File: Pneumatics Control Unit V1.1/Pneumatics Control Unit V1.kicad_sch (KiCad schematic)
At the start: 52 parts

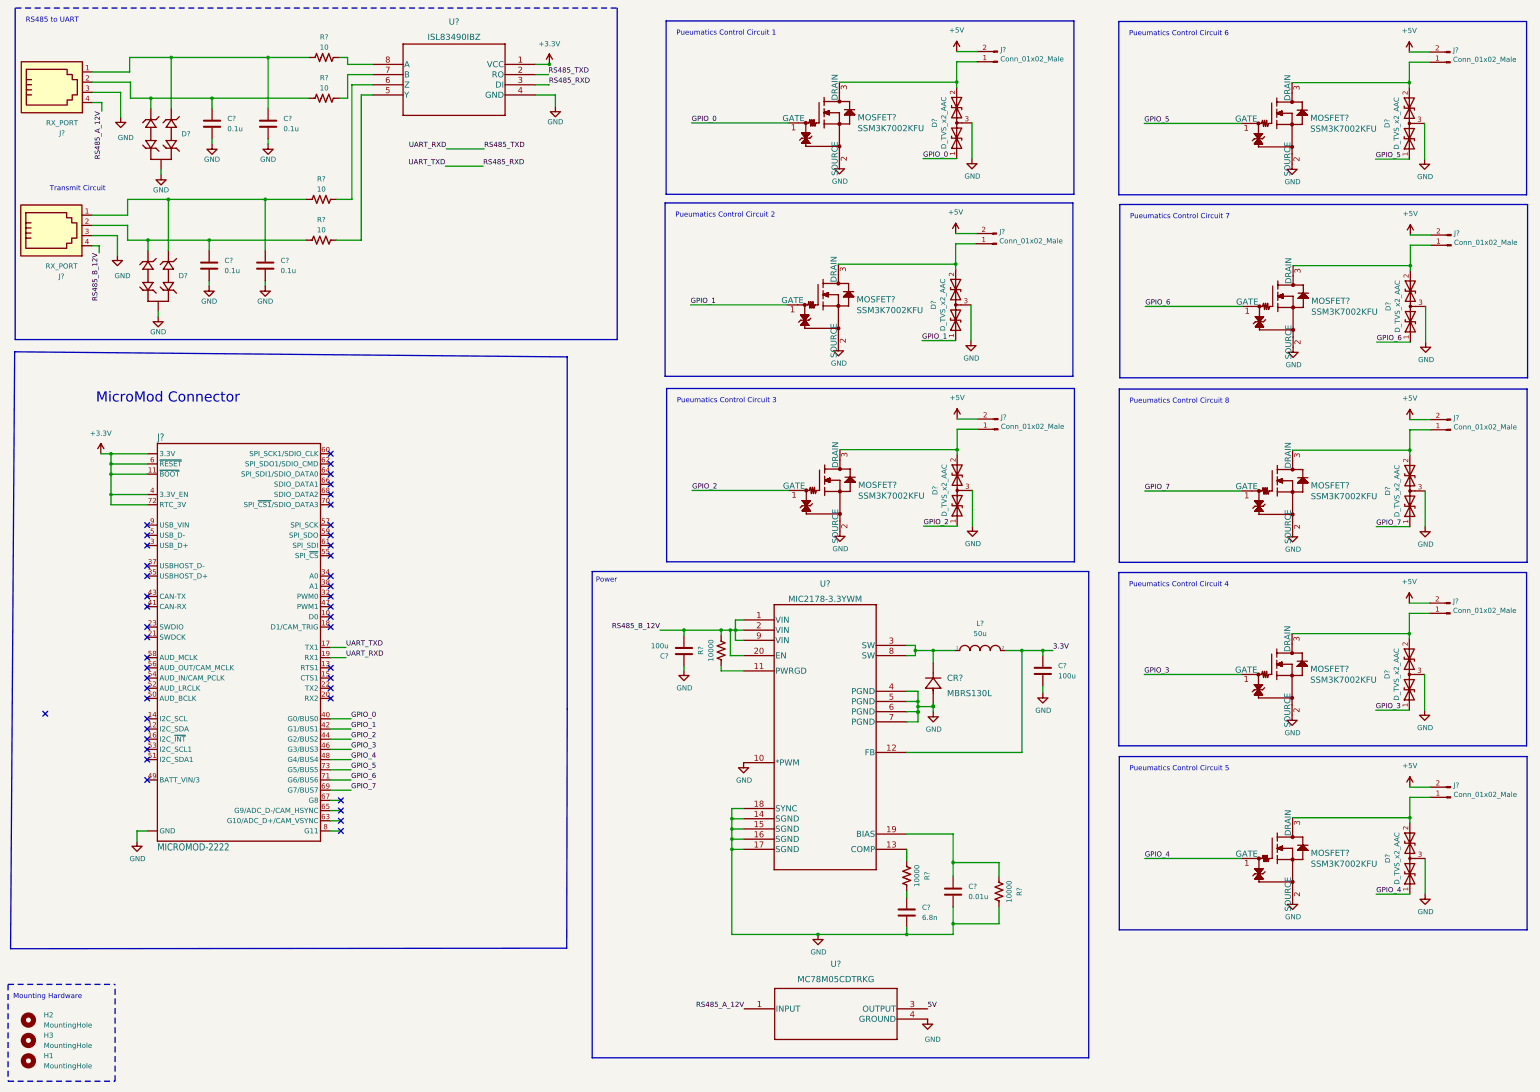
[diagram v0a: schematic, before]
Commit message: Linking foot prints
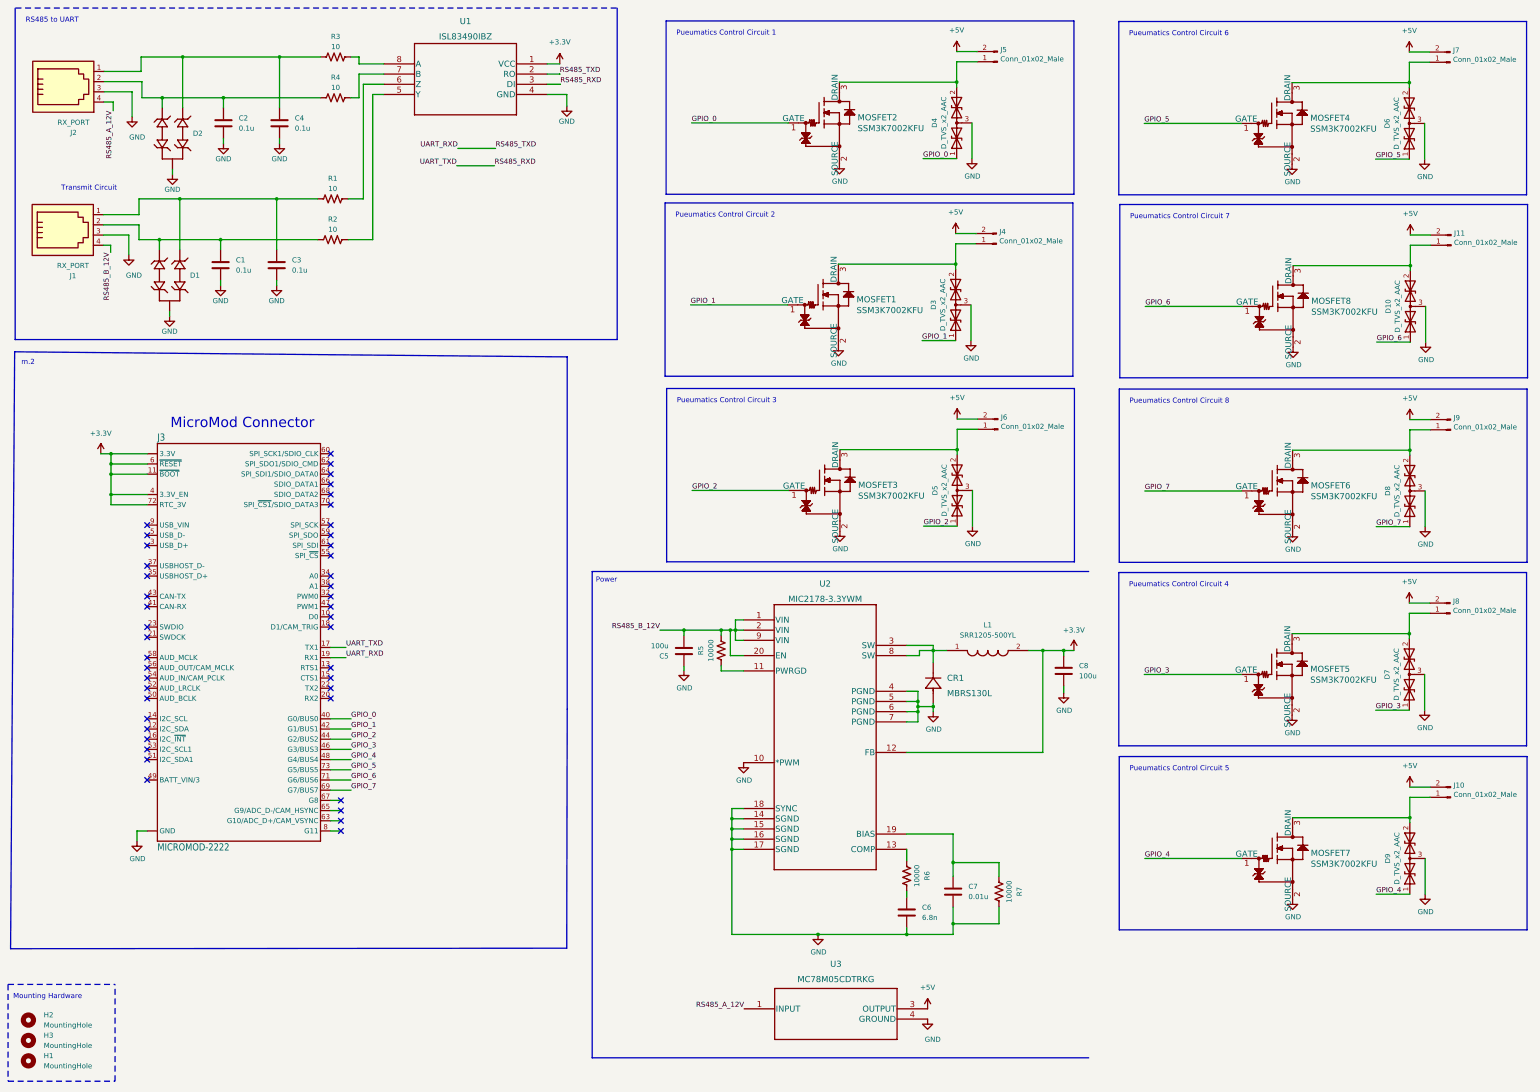
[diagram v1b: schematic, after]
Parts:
- removed L?: 50u, symbol pspice:INDUCTOR
- added L1: SRR1205-500YL, induct:SRR1205500YL, symbol induct:SRR1205-500YL
- CR1: renamed from CR?; footprint DIODE_DO214AA -> MBRS130L:MBRS130L
- J1, J2: renamed from J?; footprint Andrew_Custom:C189737 -> RS485:RS485
- J3: renamed from J?; footprint M.2-CARD-E-22 -> m2:MDT420M02001
- MOSFET1, MOSFET2, MOSFET3, MOSFET4, MOSFET5, MOSFET6, MOSFET7, MOSFET8: renamed from MOSFET?; footprint footprints:SSM3K7002KFU -> SSM3K7002KFU:SSM3K7002KFU
- U1: renamed from U?; footprint SOIC8_4X5_INR -> RS_UART:ISL83490IBZ
- U2: renamed from U?; footprint SOICW-20LD-PL-1_MCH -> 33sw:MIC2178-3.3YWM
- U3: renamed from U?; footprint DPAK-3_ONS -> 5v:MC78M05CDTRKG
- gave numbers to parts that had none: 33
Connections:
- net GND: now also CR1.2, U2.7 (PGND); no longer U1.4 (GND)
- net at CR1.1, U2.3 (SW), U2.8 (SW): now also L1.1
- net +3V3: no longer names the net of J3.11 (~{BOOT}), J3.2 (3.3V), J3.4 (3.3V_EN), J3.6 (~{RESET}), J3.72 (RTC_3V), J3.74 (3.3V)
- net +3V3: no longer U1.1 (VCC)
- removed net +5V: J10.2 (Pin_2), J11.2 (Pin_2), J4.2 (Pin_2), J5.2 (Pin_2), J6.2 (Pin_2), J7.2 (Pin_2), J8.2 (Pin_2), J9.2 (Pin_2)
- net 3.3V: no longer names the net of C8.1, U2.12 (FB)
- net 3.3V: now also L1.2
- net 5V: no longer names the net of U3.3 (OUTPUT)
- no-connect marks 45 -> 44
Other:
- note added: "m.2"
- moved on the sheet: C1, C2, C3, C4, C8, D1, D2, J1, J2, R1, R2, R3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

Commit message: Adding USB for programming, Removing linear 5V, standardizing diodes, cleaning up capcitors
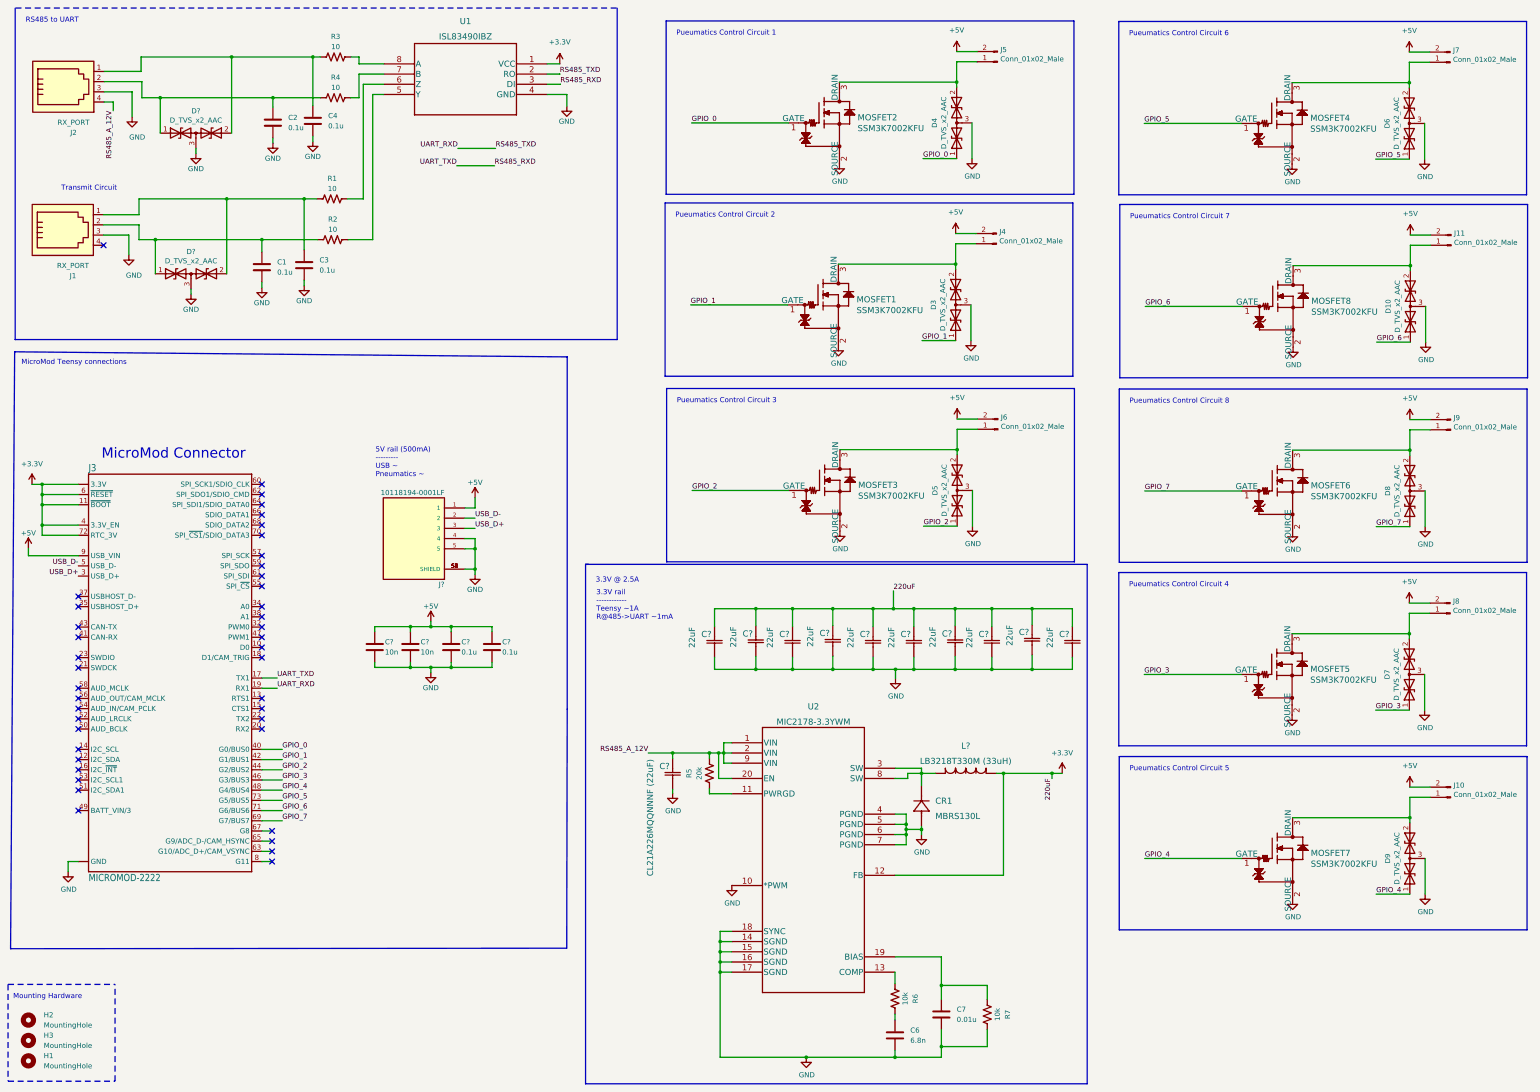
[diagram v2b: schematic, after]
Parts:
- removed C5, C8: 100u, Capacitor_SMD:C_0805_2012Metric_Pad1.18x1.45mm_HandSolder, symbol Device:C
- removed D1, D2: CDSOT23-SM712, CDSOT23-SM712:SOT-23-3, symbol CDSOT23-SM712:CDSOT23-SM712
- removed L1: SRR1205-500YL, induct:SRR1205500YL, symbol induct:SRR1205-500YL
- removed U3: MC78M05CDTRKG, 5v:MC78M05CDTRKG, symbol 2022-03-25_21-05-18:MC78M05CDTRKG
- added C? (x10): 22uF, CAP_CL21_SAM, symbol Cap22U:CL21A226MQQNNNF
- added C? (x2): 0.1u, Capacitor_SMD:C_0805_2012Metric_Pad1.18x1.45mm_HandSolder, symbol Device:C
- added C? (x2): 10n, Capacitor_SMD:C_0805_2012Metric_Pad1.18x1.45mm_HandSolder, symbol Device:C
- added C?: CL21A226MQQNNNF (22uF), CAP_CL21_SAM, symbol Cap22U:CL21A226MQQNNNF
- added D? (x2): D_TVS_x2_AAC, Package_TO_SOT_SMD:SOT-723, symbol Device:D_TVS_x2_AAC
- added J?: 10118194-0001LF, 10118194-0001LF:AMPHENOL_10118194-0001LF, symbol 10118194-0001LF:10118194-0001LF
- added L?: LB3218T330M (33uH), IND_TAIYO_LB3218_TAY, symbol induct33u:LB3218T330M
- R5: value 10000 -> 20k
- R6, R7: value 10000 -> 10k
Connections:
- net GND: now also C?.2, C?.2, C?.2, C?.2, C?.2, C?.2, C?.2, C?.2, C?.2, C?.2, C?.2, C?.2, C?.2, C?.2, C?.2, D?.3 (common), D?.3 (common), J?.4, J?.5, J?.S1 (SHIELD), J?.S2 (SHIELD), J?.S3 (SHIELD), J?.S4 (SHIELD), J?.S5 (SHIELD), J?.S6 (SHIELD)
- net RS485_A_12V: now also R5.2, U2.1 (VIN), U2.2 (VIN), U2.20 (EN), U2.9 (VIN), C?.1
- net at CR1.1, U2.3 (SW), U2.8 (SW): now also L?.2
- net at C3.1, J1.1, R1.1: now also D?.2 (A2)
- net at C1.1, J1.2, R2.1: now also D?.1 (A1)
- net at C2.1, J2.2, R4.1: now also D?.1 (A1)
- net at C4.1, J2.1, R3.1: now also D?.2 (A2)
- net 220uF: now reaches U2.12 (FB)
- net 220uF: now also C?.1, C?.1, C?.1, C?.1, C?.1, C?.1, C?.1, C?.1, C?.1, C?.1, L?.1
- net USB_D+: now reaches J3.3 (USB_D+)
- net USB_D+: now also J?.3
- net USB_D-: now reaches J3.5 (USB_D-)
- net USB_D-: now also J?.2
- net +5V: now reaches J3.9 (USB_VIN)
- net +5V: now also C?.1, C?.1, C?.1, C?.1, J?.1
- removed net RS485_B_12V: J1.4, R5.2, U2.1 (VIN), U2.2 (VIN), U2.20 (EN), U2.9 (VIN)
- no-connect marks 44 -> 42
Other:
- note added: "3.3V @ 2.5A"
- note added: "3.3V rail ------------ Teensy ~1A R@485->UART ~1mA"
- note added: "5V rail (500mA) --------- USB ~ Pneumatics ~"
- note added: "MicroMod Teensy connections"
- note removed: "Power"
- note removed: "m.2"
- moved on the sheet: C1, C2, C3, C4, C6, C7, CR1, J3, R5, R6, R7, U2

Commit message: Footprint fun
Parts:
- C11, C12, C13, C14, C15, C16, C17, C18, C19, C20, C21: renamed from C?; footprint CAP_CL21_SAM -> 22U:CL21A226MQQNNNF
- L1: renamed from L?; footprint IND_TAIYO_LB3218_TAY -> induct33u:LB3218T330M
- gave numbers to parts that had none: 7
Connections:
- net +5V: no longer names the net of C10.1, C5.1, C8.1, C9.1
- net +5V: no longer J12.1, J3.9 (USB_VIN)

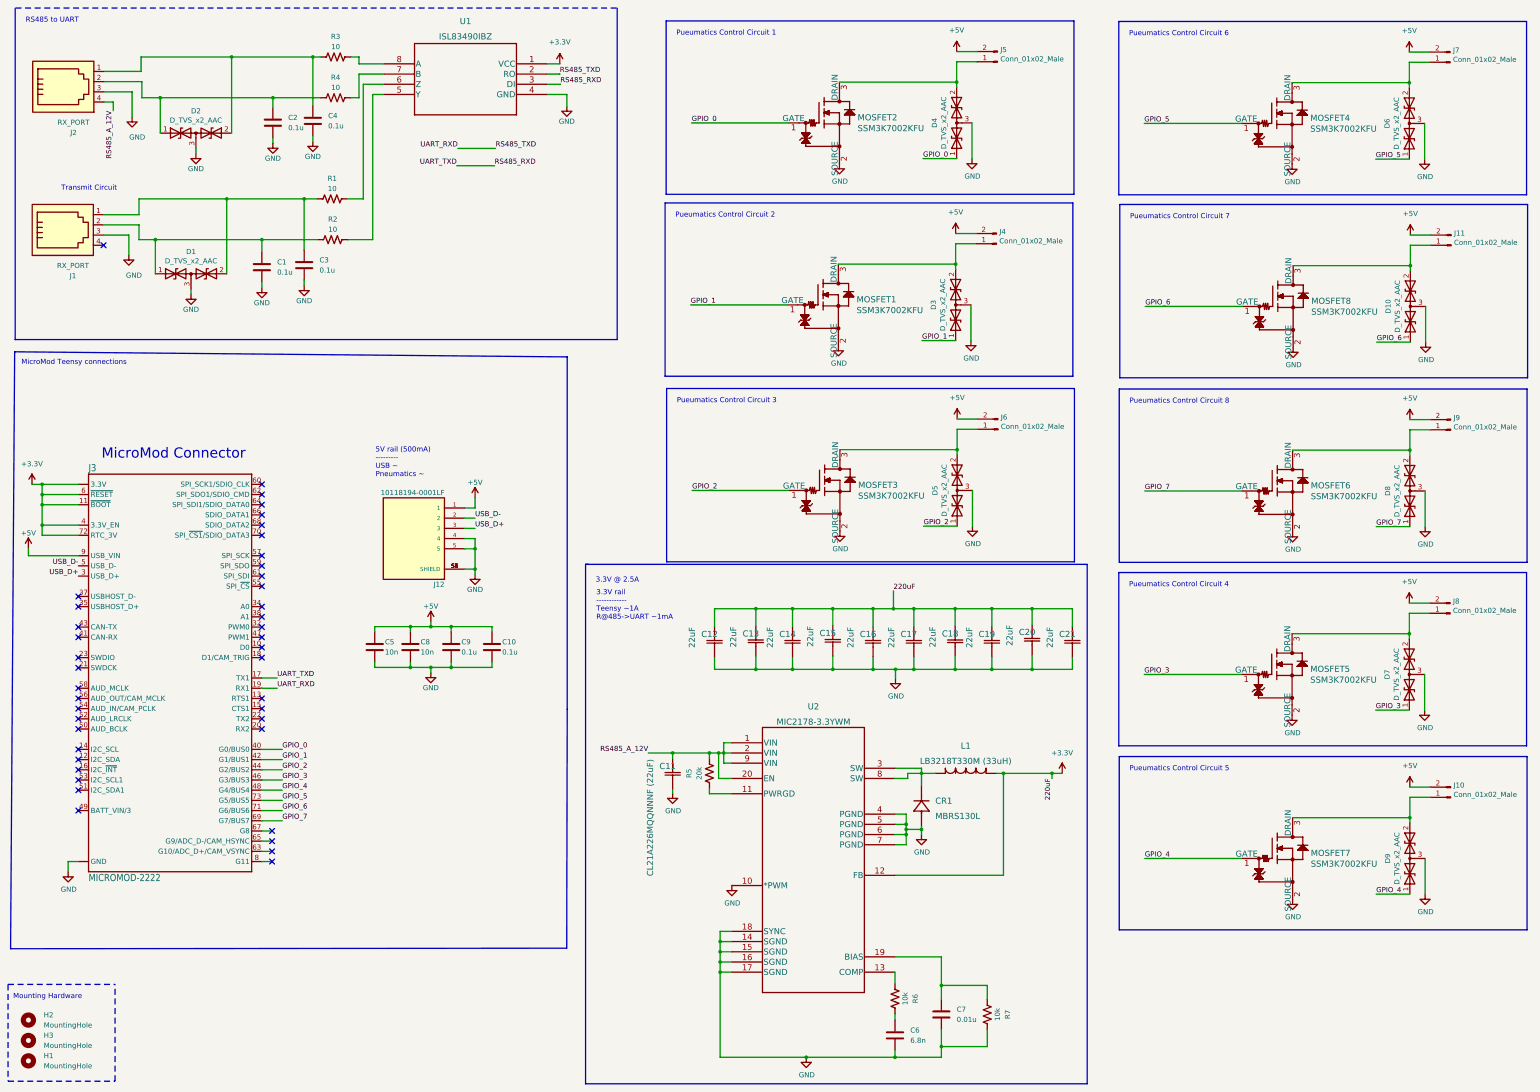
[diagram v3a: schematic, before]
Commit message: Adding back the 5V linear regulator
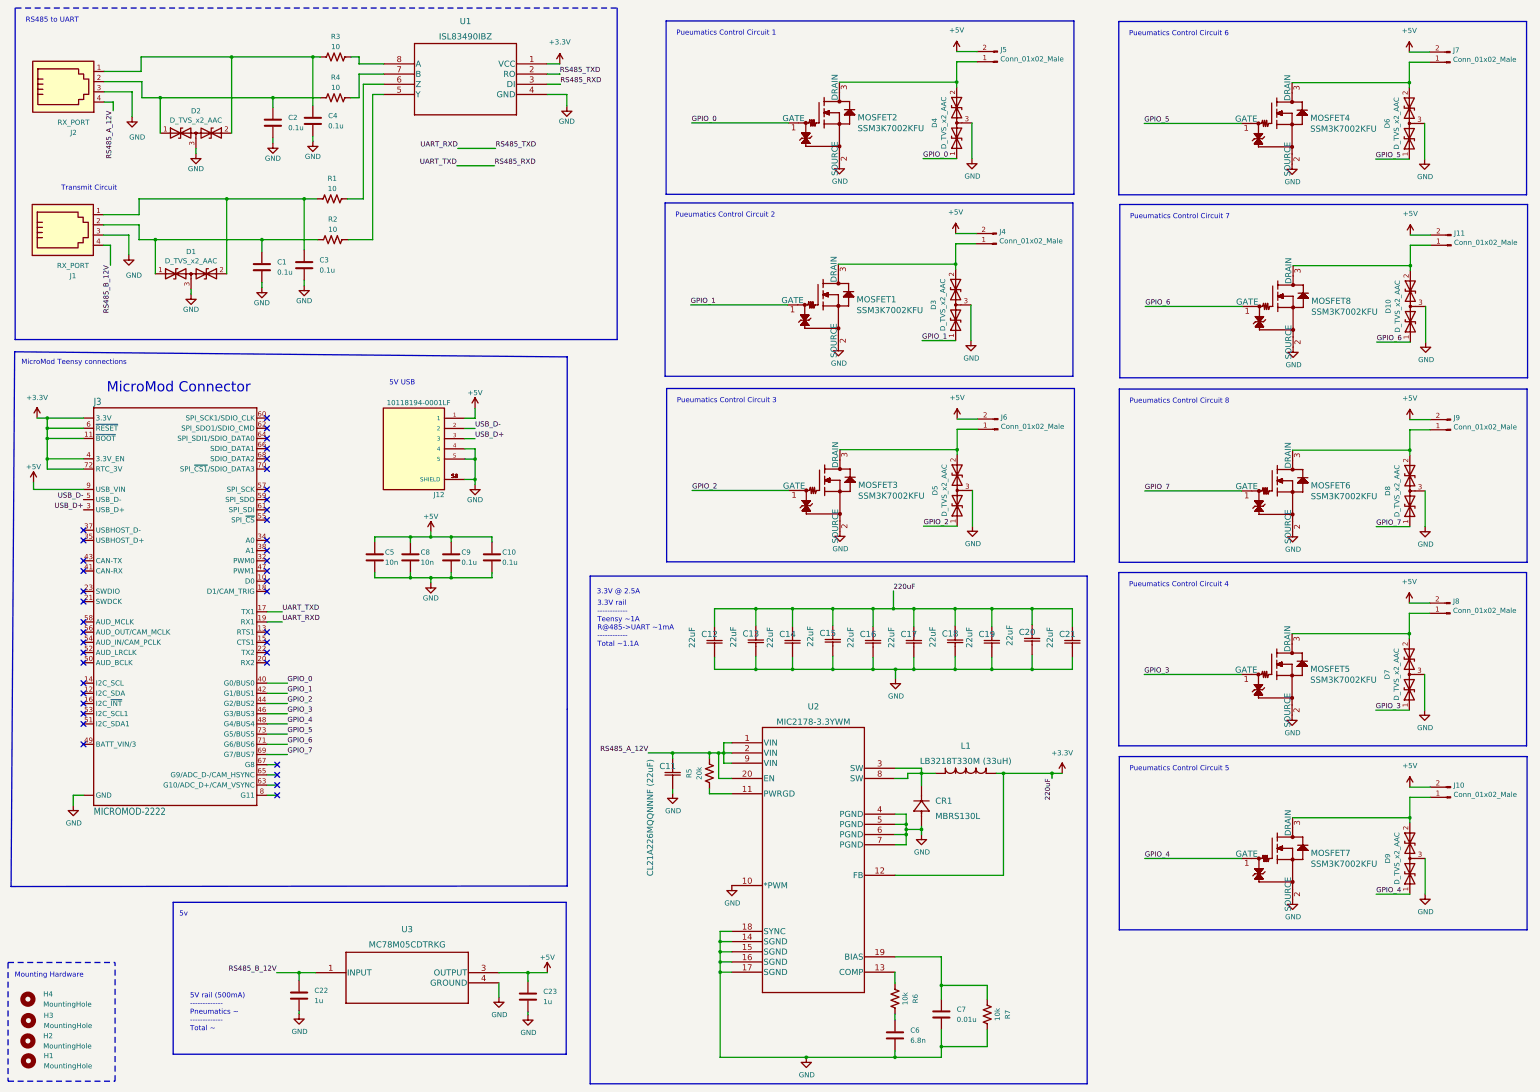
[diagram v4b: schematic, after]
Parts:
- added C22, C23: 1u, Capacitor_SMD:C_0805_2012Metric_Pad1.18x1.45mm_HandSolder, symbol Device:C
- added H4: MountingHole, MountingHole:MountingHole_2.5mm, symbol Mechanical:MountingHole
- added U3: MC78M05CDTRKG, 12v5v:MC78M05CDTRKG, symbol 12V5V:MC78M05CDTRKG
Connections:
- net GND: now also C22.2, C23.2, U3.4 (GROUND)
- net RS485_B_12V: now reaches J1.4
- net RS485_B_12V: now also C22.1, U3.1 (INPUT)
- new net: C23.1, U3.3 (OUTPUT)
- no-connect marks 42 -> 41
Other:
- note added: "3.3V rail ------------ Teensy ~1A R@485->UART ~1mA ------------ Total ~1.1A"
- note added: "5V USB"
- note added: "5V rail (500mA) ------------- Pneumatics ~ ------------- Total ~"
- note added: "5v"
- note removed: "3.3V rail ------------ Teensy ~1A R@485->UART ~1mA"
- note removed: "5V rail (500mA) --------- USB ~ Pneumatics ~"
- moved on the sheet: C10, C5, C8, C9, H2, H3, J12, J3
